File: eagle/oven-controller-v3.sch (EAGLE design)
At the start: 44 parts, among them Q1 FDV305N, Q2 FDV305N, Q3 FDV305N, Q4 FDV305N, U1 ARDUINO_SHIELDLONGPADS, U2 MAX31855, U3 MAX31855, U4 MAX31855, U5 MAX31855, U6 MAX31855, U7 SN74LVC1G139

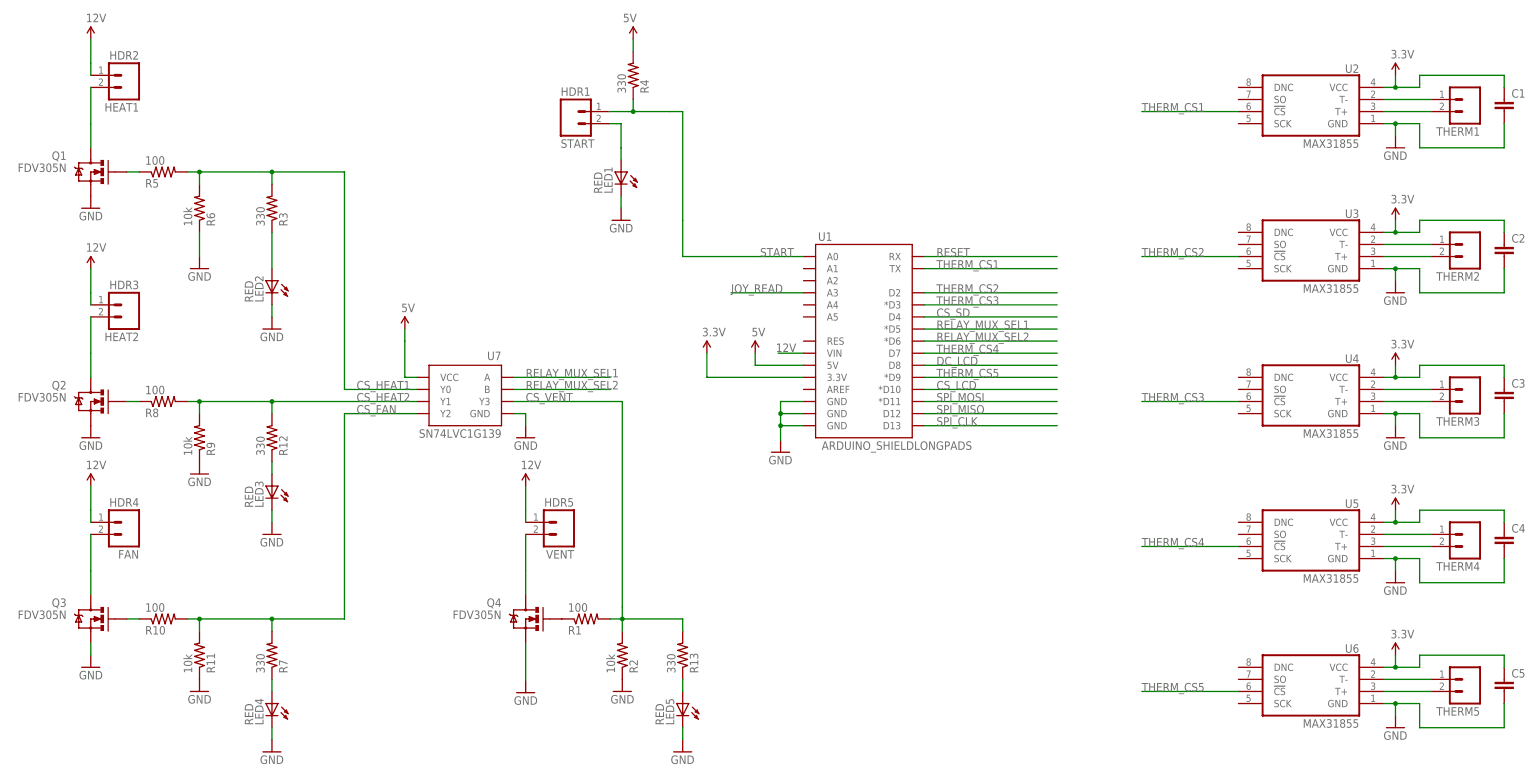
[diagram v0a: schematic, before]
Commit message: Changing directory structure.
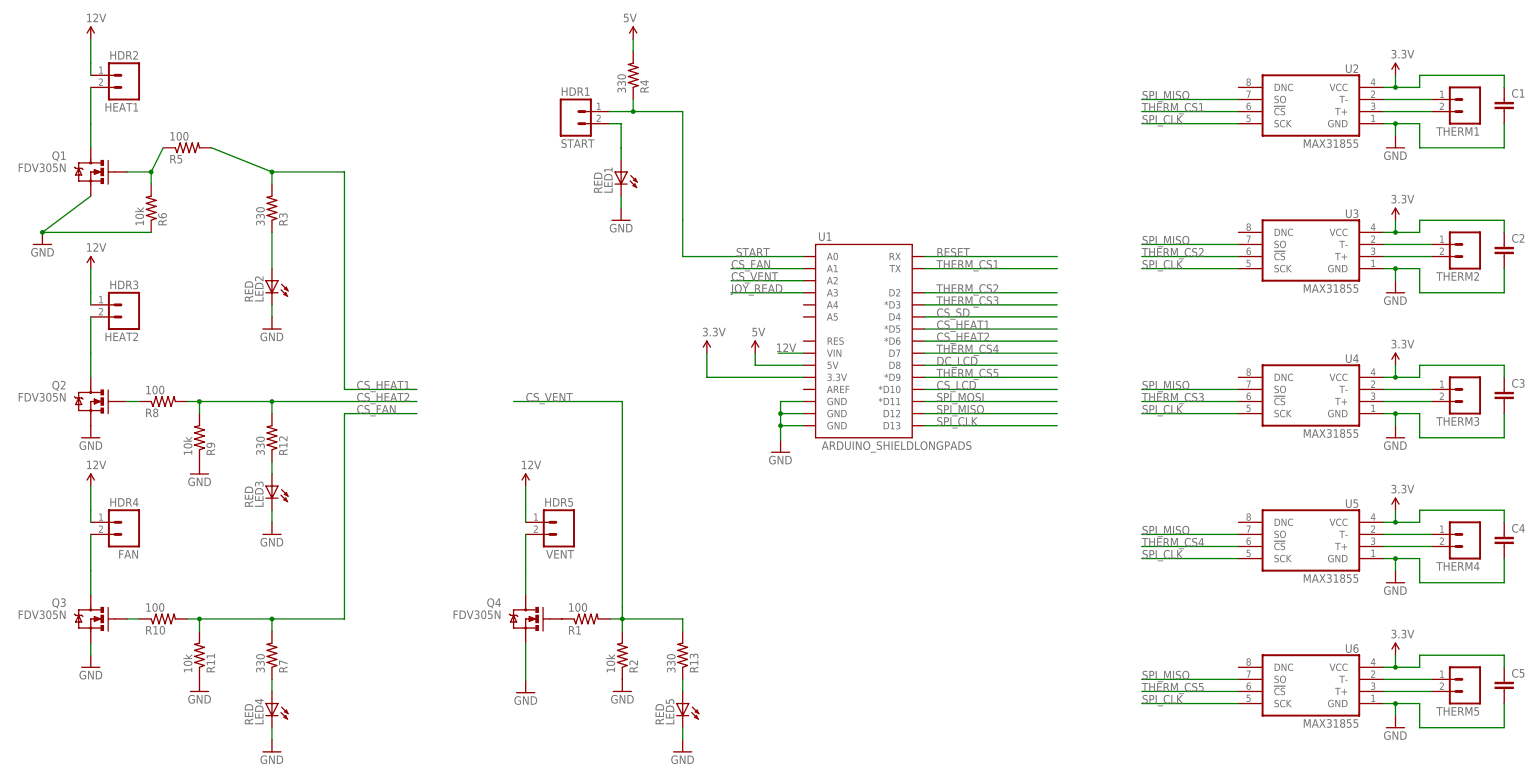
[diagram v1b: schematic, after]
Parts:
- removed U7: SN74LVC1G139, wicker:SN74LVC1G139
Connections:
- removed net RELAY_MUX_SEL1: U1.*D5, U7.A
- removed net RELAY_MUX_SEL2: U1.*D6, U7.B
- net 5V: no longer U7.VCC
- net CS_FAN: now also U1.A1; no longer U7.Y2
- net CS_HEAT1: now also U1.*D5; no longer R5.2, R6.2, U7.Y0
- net CS_HEAT2: now also U1.*D6; no longer U7.Y1
- net CS_VENT: now also U1.A2; no longer U7.Y3
- net GND: no longer U7.GND
- net N$1: now also R6.2
- net SPI_CLK: now also U2.SCK, U3.SCK, U4.SCK, U5.SCK, U6.SCK
- net SPI_MISO: now also U2.SO, U3.SO, U4.SO, U5.SO, U6.SO
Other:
- moved on the sheet: R5, R6
